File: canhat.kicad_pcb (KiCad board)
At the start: 2 copper layers, 65 x 30 mm, 36 parts, among them J1 Raspberry_Pi_2_3, J2 CAN In/Out/GND, J5 12V, U1 MCP2515-xSO, U2 SN65HVD234, U3 AT24C32-SSHM, U4 AP63205, Y1 16MHz

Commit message: Routing and tweaking
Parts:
- L1: footprint Inductor_SMD:L_Abracon_ASPI-0630LR -> onitake:DS75LC
- moved R7 35.1 mm to (101.6, 70.7), turned to 180 degrees
- moved R6 33.1 mm to (101.6, 68.8), turned to 0 degrees
- moved R9 0.44 mm to (88.6, 74.9)
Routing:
- net +5V: track 46.5 -> 88.6 mm, vias 2 -> 1
- net VBUS: track 31.4 -> 12.2 mm, vias 2 -> 0
- net /~INT: track 16.4 -> 12.7 mm
- net GND: track 31.7 -> 30.8 mm, vias 17 -> 16

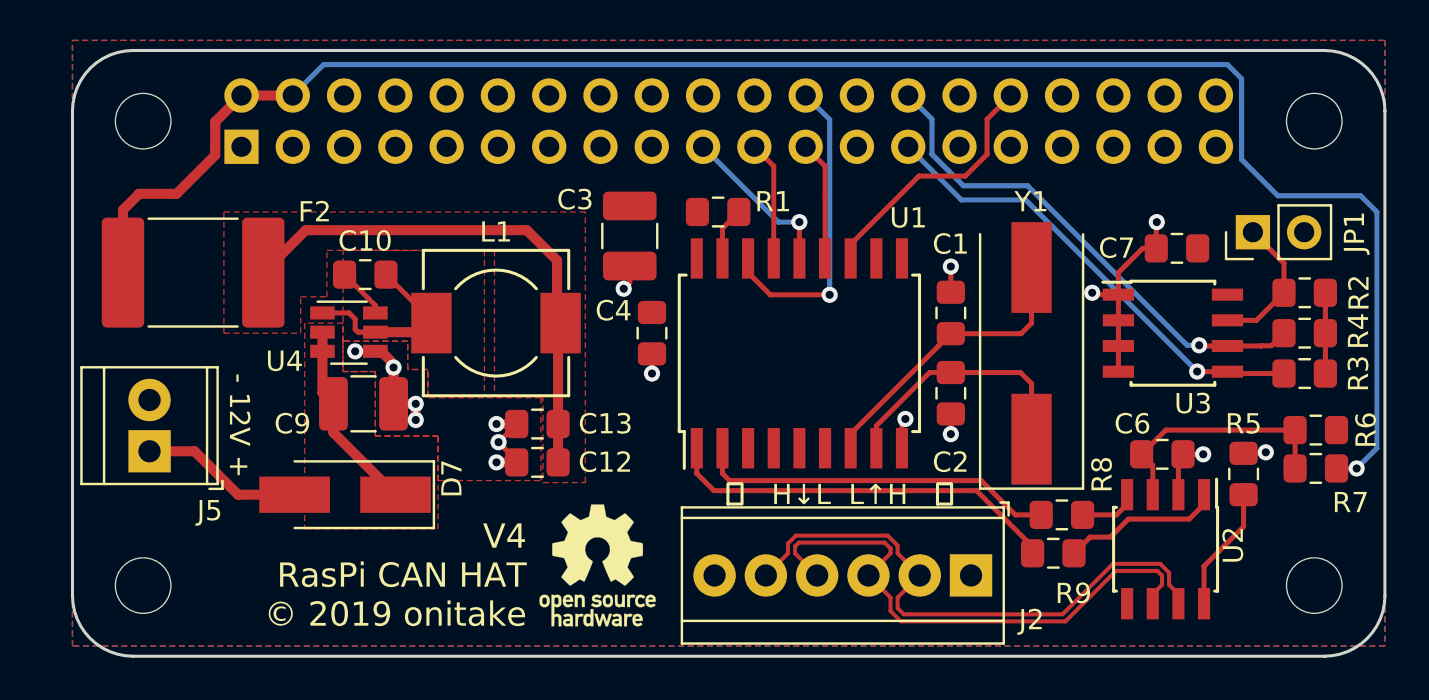
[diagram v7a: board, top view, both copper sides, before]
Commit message: Added direct-5V jumper
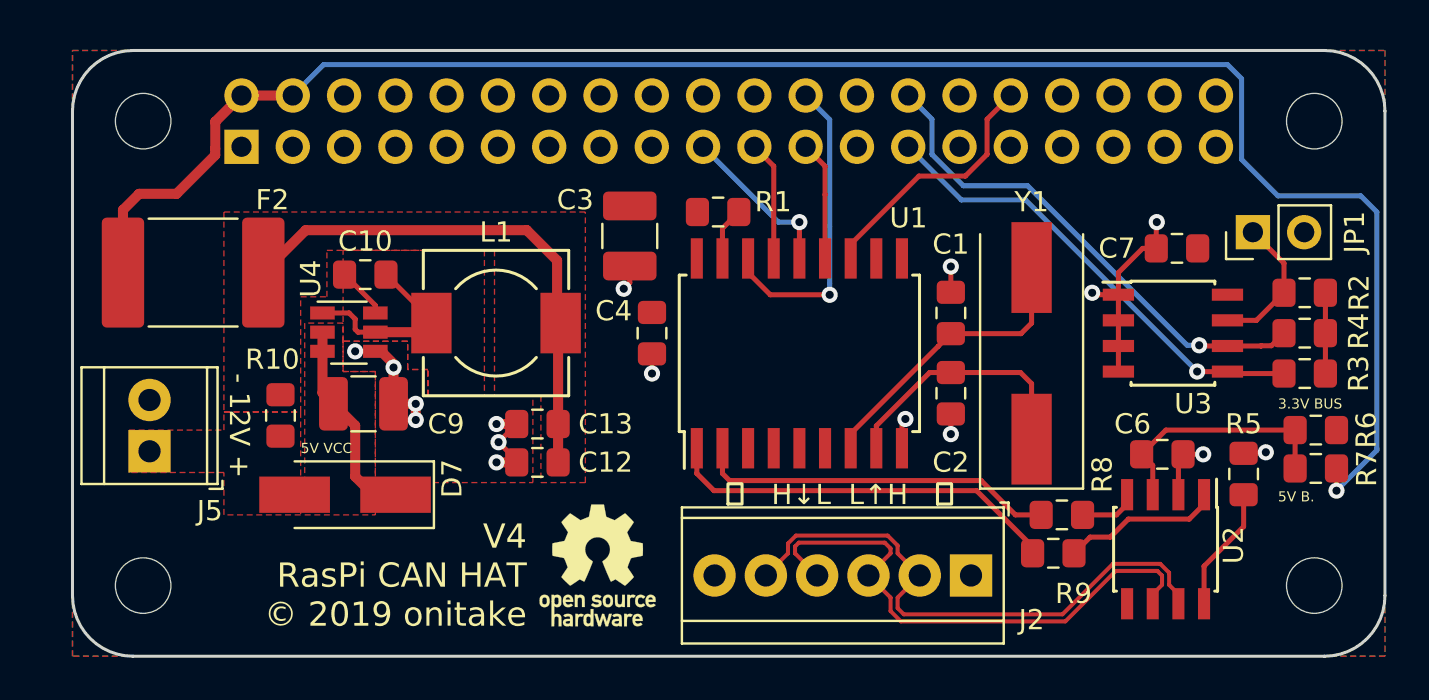
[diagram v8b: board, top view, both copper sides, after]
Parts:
- added R10: DNP/0, Resistor_SMD:R_0805_2012Metric_Pad1.15x1.40mm_HandSolder, F.Cu at (50.3, 68.1)
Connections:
- C9 pad 1: +12V -> Net-(C9-Pad1)
- D7 pad 1: +12V -> Net-(C9-Pad1)
- D7 pad 2: Net-(D7-Pad2) -> +12V
- J5 pad 1: Net-(D7-Pad2) -> +12V
- U4 pad 2: +12V -> Net-(C9-Pad1)
- U4 pad 3: +12V -> Net-(C9-Pad1)
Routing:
- net Net-(C9-Pad1): track 0.00 -> 13.2 mm
- net +12V: track 12.6 -> 0.00 mm
- net Net-(D7-Pad2): track 8.08 -> 0.00 mm
- net +5V: track 88.6 -> 90.2 mm
- added copper zone on F.Cu, net Net-(C9-Pad1)
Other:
- board text added: "3.3V BUS"
- board text added: "5V B."
- board text added: "5V VCC"
